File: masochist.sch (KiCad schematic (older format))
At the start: 76 parts, among them J1 USB_C_Receptacle_USB2.0, J2 AVR-ISP-6, SW1 RESET, SW2 SW_Push, U1 ATmega328P-PU, Y1 Crystal

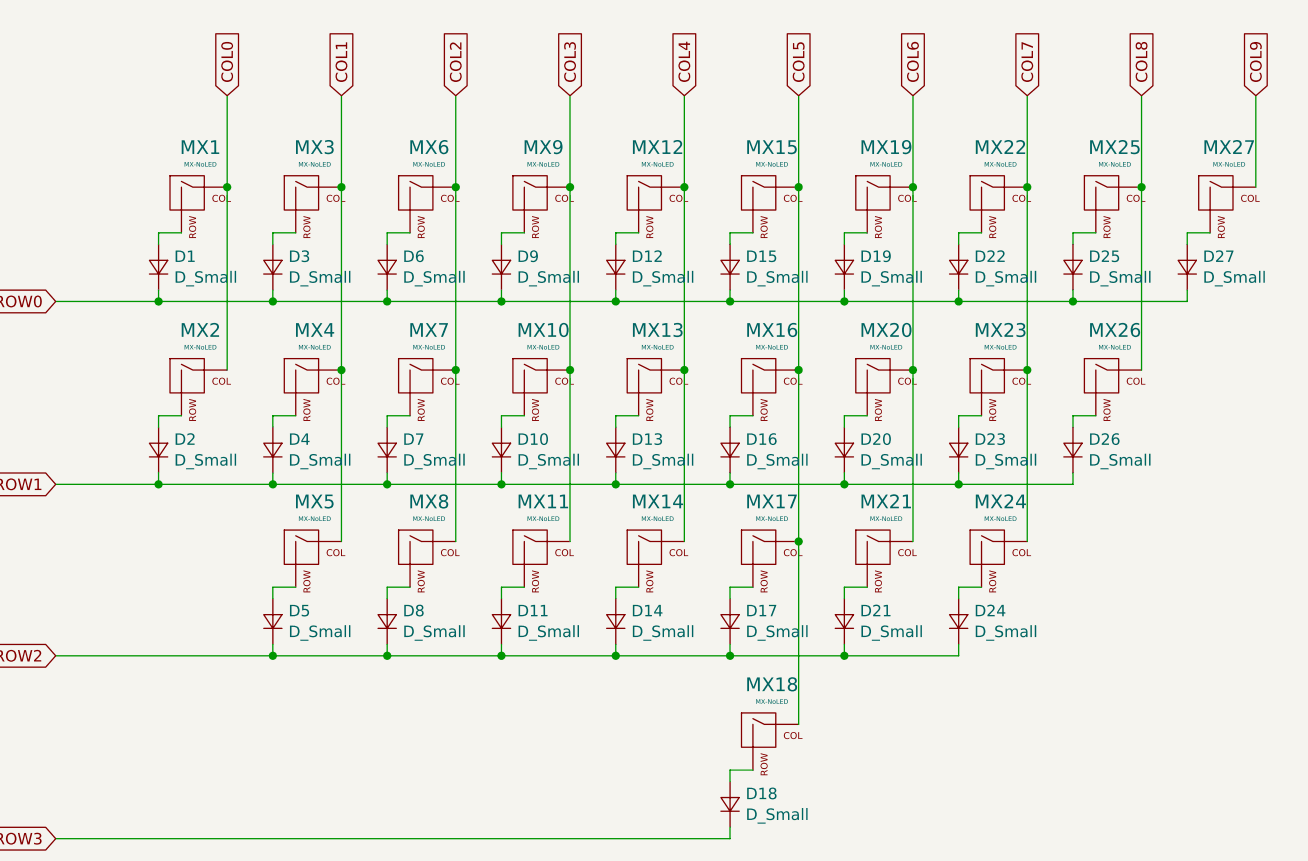
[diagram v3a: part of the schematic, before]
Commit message: laying out the switches and diodes
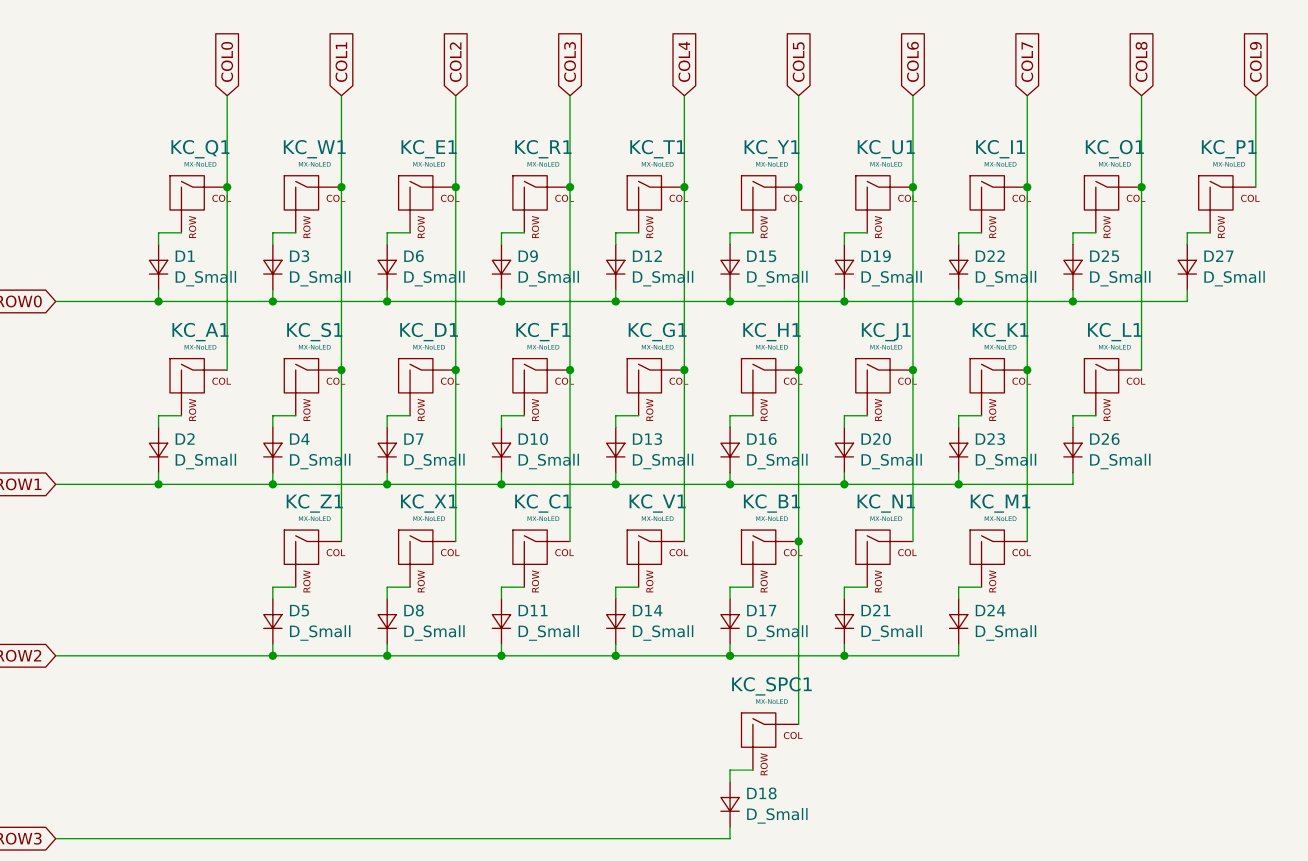
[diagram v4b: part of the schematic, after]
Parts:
- renumbered MX2 to KC_A1, MX17 to KC_B1, MX11 to KC_C1, MX7 to KC_D1, MX6 to KC_E1, MX10 to KC_F1, MX13 to KC_G1, MX16 to KC_H1, MX22 to KC_I1, MX20 to KC_J1, MX23 to KC_K1, MX26 to KC_L1, MX24 to KC_M1, MX21 to KC_N1, MX25 to KC_O1, MX27 to KC_P1, MX1 to KC_Q1, MX9 to KC_R1, MX4 to KC_S1, MX18 to KC_SPC1, MX12 to KC_T1, MX19 to KC_U1, MX14 to KC_V1, MX3 to KC_W1, MX8 to KC_X1, MX15 to KC_Y1, MX5 to KC_Z1
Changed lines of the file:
@@
 	1500 3900 1500 4050
 $Comp
-L MX_Alps_Hybrid:MX-NoLED MX1
+L MX_Alps_Hybrid:MX-NoLED KC_Q1
 U 1 1 5EC3FB15
 P 6450 1200
-F 0 "MX1" H 6483 1423 60  0000 C CNN
+F 0 "KC_Q1" H 6483 1423 60  0000 C CNN
 F 1 "MX-NoLED" H 6483 1349 20  0000 C CNN
 F 2 "cftkb:SW_Cherry_MX1A_1.00u_PCB-NOSCREEN" H 5825 1175 60  0001 C CNN
@@
 	6300 1350 6400 1350
 $Comp
-L MX_Alps_Hybrid:MX-NoLED MX3
+L MX_Alps_Hybrid:MX-NoLED KC_W1
 U 1 1 5EC70529
 P 6950 1200
-F 0 "MX3" H 6983 1423 60  0000 C CNN
+F 0 "KC_W1" H 6983 1423 60  0000 C CNN
 F 1 "MX-NoLED" H 6983 1349 20  0000 C CNN
 F 2 "cftkb:SW_Cherry_MX1A_1.00u_PCB-NOSCREEN" H 6325 1175 60  0001 C CNN
@@
 	6800 1350 6900 1350
 $Comp
-L MX_Alps_Hybrid:MX-NoLED MX6
+L MX_Alps_Hybrid:MX-NoLED KC_E1
 U 1 1 5EC71EA7
 P 7450 1200
-F 0 "MX6" H 7483 1423 60  0000 C CNN
+F 0 "KC_E1" H 7483 1423 60  0000 C CNN
 F 1 "MX-NoLED" H 7483 1349 20  0000 C CNN
 F 2 "cftkb:SW_Cherry_MX1A_1.00u_PCB-NOSCREEN" H 6825 1175 60  0001 C CNN
@@
 	7300 1350 7400 1350
 $Comp
-L MX_Alps_Hybrid:MX-NoLED MX9
+L MX_Alps_Hybrid:MX-NoLED KC_R1
 U 1 1 5EC71EB5
 P 7950 1200
-F 0 "MX9" H 7983 1423 60  0000 C CNN
+F 0 "KC_R1" H 7983 1423 60  0000 C CNN
 F 1 "MX-NoLED" H 7983 1349 20  0000 C CNN
 F 2 "cftkb:SW_Cherry_MX1A_1.00u_PCB-NOSCREEN" H 7325 1175 60  0001 C CNN
@@
 	7800 1350 7900 1350
 $Comp
-L MX_Alps_Hybrid:MX-NoLED MX12
+L MX_Alps_Hybrid:MX-NoLED KC_T1
 U 1 1 5EC74ECF
 P 8450 1200
-F 0 "MX12" H 8483 1423 60  0000 C CNN
+F 0 "KC_T1" H 8483 1423 60  0000 C CNN
 F 1 "MX-NoLED" H 8483 1349 20  0000 C CNN
 F 2 "cftkb:SW_Cherry_MX1A_1.00u_PCB-NOSCREEN" H 7825 1175 60  0001 C CNN
@@
 	8300 1350 8400 1350
 $Comp
-L MX_Alps_Hybrid:MX-NoLED MX15
+L MX_Alps_Hybrid:MX-NoLED KC_Y1
 U 1 1 5EC74EDD
 P 8950 1200
-F 0 "MX15" H 8983 1423 60  0000 C CNN
+F 0 "KC_Y1" H 8983 1423 60  0000 C CNN
 F 1 "MX-NoLED" H 8983 1349 20  0000 C CNN
 F 2 "cftkb:SW_Cherry_MX1A_1.00u_PCB-NOSCREEN" H 8325 1175 60  0001 C CNN
@@
 	8800 1350 8900 1350
 $Comp
-L MX_Alps_Hybrid:MX-NoLED MX19
+L MX_Alps_Hybrid:MX-NoLED KC_U1
 U 1 1 5EC74EEB
 P 9450 1200
-F 0 "MX19" H 9483 1423 60  0000 C CNN
+F 0 "KC_U1" H 9483 1423 60  0000 C CNN
 F 1 "MX-NoLED" H 9483 1349 20  0000 C CNN
 F 2 "cftkb:SW_Cherry_MX1A_1.00u_PCB-NOSCREEN" H 8825 1175 60  0001 C CNN
@@
 	9300 1350 9400 1350
 $Comp
-L MX_Alps_Hybrid:MX-NoLED MX22
+L MX_Alps_Hybrid:MX-NoLED KC_I1
 U 1 1 5EC74EF9
 P 9950 1200
-F 0 "MX22" H 9983 1423 60  0000 C CNN
+F 0 "KC_I1" H 9983 1423 60  0000 C CNN
 F 1 "MX-NoLED" H 9983 1349 20  0000 C CNN
 F 2 "cftkb:SW_Cherry_MX1A_1.00u_PCB-NOSCREEN" H 9325 1175 60  0001 C CNN
@@
 	9800 1350 9900 1350
 $Comp
-L MX_Alps_Hybrid:MX-NoLED MX25
+L MX_Alps_Hybrid:MX-NoLED KC_O1
 U 1 1 5EC76445
 P 10450 1200
-F 0 "MX25" H 10483 1423 60  0000 C CNN
+F 0 "KC_O1" H 10483 1423 60  0000 C CNN
 F 1 "MX-NoLED" H 10483 1349 20  0000 C CNN
 F 2 "cftkb:SW_Cherry_MX1A_1.00u_PCB-NOSCREEN" H 9825 1175 60  0001 C CNN
@@
 	10300 1350 10400 1350
 $Comp
-L MX_Alps_Hybrid:MX-NoLED MX27
+L MX_Alps_Hybrid:MX-NoLED KC_P1
 U 1 1 5EC76453
 P 10950 1200
-F 0 "MX27" H 10983 1423 60  0000 C CNN
+F 0 "KC_P1" H 10983 1423 60  0000 C CNN
 F 1 "MX-NoLED" H 10983 1349 20  0000 C CNN
 F 2 "cftkb:SW_Cherry_MX1A_1.00u_PCB-NOSCREEN" H 10325 1175 60  0001 C CNN
@@
 	10800 1350 10900 1350
 $Comp
-L MX_Alps_Hybrid:MX-NoLED MX2
+L MX_Alps_Hybrid:MX-NoLED KC_A1
 U 1 1 5EC84E7F
 P 6450 2000
-F 0 "MX2" H 6483 2223 60  0000 C CNN
+F 0 "KC_A1" H 6483 2223 60  0000 C CNN
 F 1 "MX-NoLED" H 6483 2149 20  0000 C CNN
 F 2 "cftkb:SW_Cherry_MX1A_1.00u_PCB-NOSCREEN" H 5825 1975 60  0001 C CNN
@@
 	6300 2150 6400 2150
 $Comp
-L MX_Alps_Hybrid:MX-NoLED MX4
+L MX_Alps_Hybrid:MX-NoLED KC_S1
 U 1 1 5EC84E8D
 P 6950 2000
-F 0 "MX4" H 6983 2223 60  0000 C CNN
+F 0 "KC_S1" H 6983 2223 60  0000 C CNN
 F 1 "MX-NoLED" H 6983 2149 20  0000 C CNN
 F 2 "cftkb:SW_Cherry_MX1A_1.00u_PCB-NOSCREEN" H 6325 1975 60  0001 C CNN
@@
 	6800 2150 6900 2150
 $Comp
-L MX_Alps_Hybrid:MX-NoLED MX7
+L MX_Alps_Hybrid:MX-NoLED KC_D1
 U 1 1 5EC84E9B
 P 7450 2000
-F 0 "MX7" H 7483 2223 60  0000 C CNN
+F 0 "KC_D1" H 7483 2223 60  0000 C CNN
 F 1 "MX-NoLED" H 7483 2149 20  0000 C CNN
 F 2 "cftkb:SW_Cherry_MX1A_1.00u_PCB-NOSCREEN" H 6825 1975 60  0001 C CNN
@@
 	7300 2150 7400 2150
 $Comp
-L MX_Alps_Hybrid:MX-NoLED MX10
+L MX_Alps_Hybrid:MX-NoLED KC_F1
 U 1 1 5EC84EA9
 P 7950 2000
-F 0 "MX10" H 7983 2223 60  0000 C CNN
+F 0 "KC_F1" H 7983 2223 60  0000 C CNN
 F 1 "MX-NoLED" H 7983 2149 20  0000 C CNN
 F 2 "cftkb:SW_Cherry_MX1A_1.00u_PCB-NOSCREEN" H 7325 1975 60  0001 C CNN
@@
 	7800 2150 7900 2150
 $Comp
-L MX_Alps_Hybrid:MX-NoLED MX13
+L MX_Alps_Hybrid:MX-NoLED KC_G1
 U 1 1 5EC84EB7
 P 8450 2000
-F 0 "MX13" H 8483 2223 60  0000 C CNN
+F 0 "KC_G1" H 8483 2223 60  0000 C CNN
 F 1 "MX-NoLED" H 8483 2149 20  0000 C CNN
 F 2 "cftkb:SW_Cherry_MX1A_1.00u_PCB-NOSCREEN" H 7825 1975 60  0001 C CNN
@@
 	8300 2150 8400 2150
 $Comp
-L MX_Alps_Hybrid:MX-NoLED MX16
+L MX_Alps_Hybrid:MX-NoLED KC_H1
 U 1 1 5EC84EC5
 P 8950 2000
-F 0 "MX16" H 8983 2223 60  0000 C CNN
+F 0 "KC_H1" H 8983 2223 60  0000 C CNN
 F 1 "MX-NoLED" H 8983 2149 20  0000 C CNN
 F 2 "cftkb:SW_Cherry_MX1A_1.00u_PCB-NOSCREEN" H 8325 1975 60  0001 C CNN
@@
 	8800 2150 8900 2150
 $Comp
-L MX_Alps_Hybrid:MX-NoLED MX20
+L MX_Alps_Hybrid:MX-NoLED KC_J1
 U 1 1 5EC84ED3
 P 9450 2000
-F 0 "MX20" H 9483 2223 60  0000 C CNN
+F 0 "KC_J1" H 9483 2223 60  0000 C CNN
 F 1 "MX-NoLED" H 9483 2149 20  0000 C CNN
 F 2 "cftkb:SW_Cherry_MX1A_1.00u_PCB-NOSCREEN" H 8825 1975 60  0001 C CNN
@@
 	9300 2150 9400 2150
 $Comp
-L MX_Alps_Hybrid:MX-NoLED MX23
+L MX_Alps_Hybrid:MX-NoLED KC_K1
 U 1 1 5EC84EE1
 P 9950 2000
-F 0 "MX23" H 9983 2223 60  0000 C CNN
+F 0 "KC_K1" H 9983 2223 60  0000 C CNN
 F 1 "MX-NoLED" H 9983 2149 20  0000 C CNN
 F 2 "cftkb:SW_Cherry_MX1A_1.00u_PCB-NOSCREEN" H 9325 1975 60  0001 C CNN
@@
 	9800 2150 9900 2150
 $Comp
-L MX_Alps_Hybrid:MX-NoLED MX26
+L MX_Alps_Hybrid:MX-NoLED KC_L1
 U 1 1 5EC84EEF
 P 10450 2000
-F 0 "MX26" H 10483 2223 60  0000 C CNN
+F 0 "KC_L1" H 10483 2223 60  0000 C CNN
 F 1 "MX-NoLED" H 10483 2149 20  0000 C CNN
 F 2 "cftkb:SW_Cherry_MX1A_1.00u_PCB-NOSCREEN" H 9825 1975 60  0001 C CNN
@@
 	10300 2200 10300 2150
 $Comp
-L MX_Alps_Hybrid:MX-NoLED MX5
+L MX_Alps_Hybrid:MX-NoLED KC_Z1
 U 1 1 5EC9C168
 P 6950 2750
-F 0 "MX5" H 6983 2973 60  0000 C CNN
+F 0 "KC_Z1" H 6983 2973 60  0000 C CNN
 F 1 "MX-NoLED" H 6983 2899 20  0000 C CNN
 F 2 "cftkb:SW_Cherry_MX1A_1.00u_PCB-NOSCREEN" H 6325 2725 60  0001 C CNN
@@
 	6800 2900 6900 2900
 $Comp
-L MX_Alps_Hybrid:MX-NoLED MX8
+L MX_Alps_Hybrid:MX-NoLED KC_X1
 U 1 1 5EC9C176
 P 7450 2750
-F 0 "MX8" H 7483 2973 60  0000 C CNN
+F 0 "KC_X1" H 7483 2973 60  0000 C CNN
 F 1 "MX-NoLED" H 7483 2899 20  0000 C CNN
 F 2 "cftkb:SW_Cherry_MX1A_1.00u_PCB-NOSCREEN" H 6825 2725 60  0001 C CNN
@@
 	7300 2900 7400 2900
 $Comp
-L MX_Alps_Hybrid:MX-NoLED MX11
+L MX_Alps_Hybrid:MX-NoLED KC_C1
 U 1 1 5EC9C184
 P 7950 2750
-F 0 "MX11" H 7983 2973 60  0000 C CNN
+F 0 "KC_C1" H 7983 2973 60  0000 C CNN
 F 1 "MX-NoLED" H 7983 2899 20  0000 C CNN
 F 2 "cftkb:SW_Cherry_MX1A_1.00u_PCB-NOSCREEN" H 7325 2725 60  0001 C CNN
@@
 	7800 2900 7900 2900
 $Comp
-L MX_Alps_Hybrid:MX-NoLED MX14
+L MX_Alps_Hybrid:MX-NoLED KC_V1
 U 1 1 5EC9C192
 P 8450 2750
-F 0 "MX14" H 8483 2973 60  0000 C CNN
+F 0 "KC_V1" H 8483 2973 60  0000 C CNN
 F 1 "MX-NoLED" H 8483 2899 20  0000 C CNN
 F 2 "cftkb:SW_Cherry_MX1A_1.00u_PCB-NOSCREEN" H 7825 2725 60  0001 C CNN
@@
 	8300 2900 8400 2900
 $Comp
-L MX_Alps_Hybrid:MX-NoLED MX17
+L MX_Alps_Hybrid:MX-NoLED KC_B1
 U 1 1 5EC9C1A0
 P 8950 2750
-F 0 "MX17" H 8983 2973 60  0000 C CNN
+F 0 "KC_B1" H 8983 2973 60  0000 C CNN
 F 1 "MX-NoLED" H 8983 2899 20  0000 C CNN
 F 2 "cftkb:SW_Cherry_MX1A_1.00u_PCB-NOSCREEN" H 8325 2725 60  0001 C CNN
@@
 	8800 2900 8900 2900
 $Comp
-L MX_Alps_Hybrid:MX-NoLED MX21
+L MX_Alps_Hybrid:MX-NoLED KC_N1
 U 1 1 5EC9C1AE
 P 9450 2750
-F 0 "MX21" H 9483 2973 60  0000 C CNN
+F 0 "KC_N1" H 9483 2973 60  0000 C CNN
 F 1 "MX-NoLED" H 9483 2899 20  0000 C CNN
 F 2 "cftkb:SW_Cherry_MX1A_1.00u_PCB-NOSCREEN" H 8825 2725 60  0001 C CNN
@@
 	9300 2900 9400 2900
 $Comp
-L MX_Alps_Hybrid:MX-NoLED MX24
+L MX_Alps_Hybrid:MX-NoLED KC_M1
 U 1 1 5EC9C1BC
 P 9950 2750
-F 0 "MX24" H 9983 2973 60  0000 C CNN
+F 0 "KC_M1" H 9983 2973 60  0000 C CNN
 F 1 "MX-NoLED" H 9983 2899 20  0000 C CNN
 F 2 "cftkb:SW_Cherry_MX1A_1.00u_PCB-NOSCREEN" H 9325 2725 60  0001 C CNN
@@
 	9800 3200 9300 3200
 $Comp
-L MX_Alps_Hybrid:MX-NoLED MX18
+L MX_Alps_Hybrid:MX-NoLED KC_SPC1
 U 1 1 5ECAC523
 P 8950 3550
-F 0 "MX18" H 8983 3773 60  0000 C CNN
+F 0 "KC_SPC1" H 8983 3773 60  0000 C CNN
 F 1 "MX-NoLED" H 8983 3699 20  0000 C CNN
 F 2 "cftkb:SW_Cherry_MX1A_1.00u_PCB-NOSCREEN" H 8325 3525 60  0001 C CNN

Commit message: Project is NOT dead, components are roughly in place
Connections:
- net D+: now also U1.4 (PD2)
- net D-: now also U1.5 (PD3)
- no-connect marks 8 -> 6
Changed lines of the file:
@@
 $EndDescr
-$Comp
-L MCU_Microchip_ATmega:ATmega328P-PU U1
-U 1 1 5EC3BFE1
-P 1500 2400
-F 0 "U1" H 856 2446 50  0000 R CNN
-F 1 "ATmega328P-PU" H 856 2355 50  0000 R CNN
-F 2 "Package_DIP:DIP-28_W7.62mm" H 1500 2400 50  0001 C CIN
-F 3 "http://ww1.microchip.com/downloads/en/DeviceDoc/ATmega328_P%20AVR%20MCU%20with%20picoPower%20Technology%20Data%20Sheet%2040001984A.pdf" H 1500 2400 50  0001 C CNN
-	1    1500 2400
-	1    0    0    -1
-$EndComp
 $Comp
 L power:GND #PWR0101
@@
 NoConn ~ 2100 3500
 NoConn ~ 2100 3400
-NoConn ~ 2100 3200
-NoConn ~ 2100 3100
 NoConn ~ 900  1200
+$Comp
+L MCU_Microchip_ATmega:ATmega328P-PU U1
+U 1 1 5EC3BFE1
+P 1500 2400
+F 0 "U1" H 856 2446 50  0000 R CNN
+F 1 "ATmega328P-PU" H 856 2355 50  0000 R CNN
+F 2 "Package_DIP:DIP-28_W7.62mm" H 1500 2400 50  0001 C CIN
+F 3 "http://ww1.microchip.com/downloads/en/DeviceDoc/ATmega328_P%20AVR%20MCU%20with%20picoPower%20Technology%20Data%20Sheet%2040001984A.pdf" H 1500 2400 50  0001 C CNN
+	1    1500 2400
+	1    0    0    -1
+$EndComp
+Text GLabel 2100 3100 2    50   Input ~ 0
+D+
+Text GLabel 2100 3200 2    50   Input ~ 0
+D-
 $EndSCHEMATC

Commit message: More traces (switches and matrix diodes)
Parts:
- KC_SPC1: footprint cftkb:SW_Cherry_MX1A_1.00u_PCB-NOSCREEN -> MX_Only:MXOnly-6.25U-NoLED
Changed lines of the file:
@@
 F 0 "KC_SPC1" H 8983 3773 60  0000 C CNN
 F 1 "MX-NoLED" H 8983 3699 20  0000 C CNN
-F 2 "cftkb:SW_Cherry_MX1A_1.00u_PCB-NOSCREEN" H 8325 3525 60  0001 C CNN
+F 2 "MX_Only:MXOnly-6.25U-NoLED" H 8325 3525 60  0001 C CNN
 F 3 "" H 8325 3525 60  0001 C CNN
 	1    8950 3550

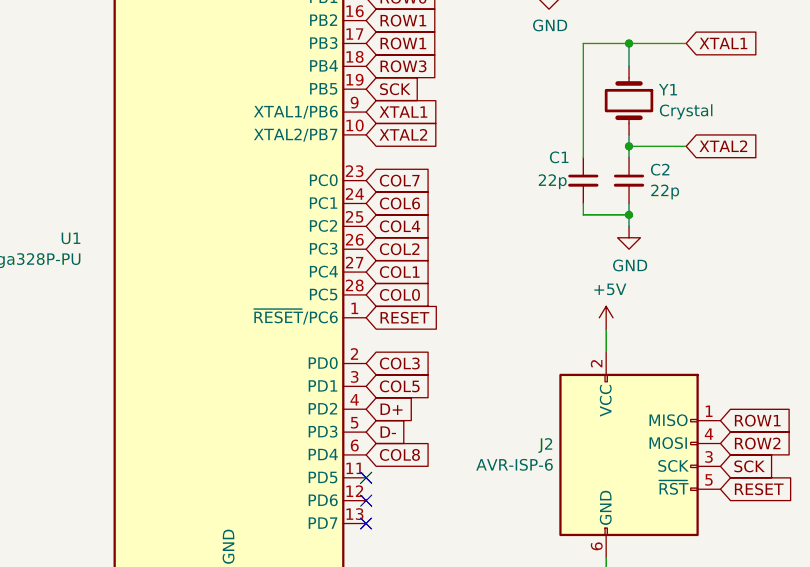
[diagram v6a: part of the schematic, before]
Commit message: reassigning pins to hopefully make routing easier
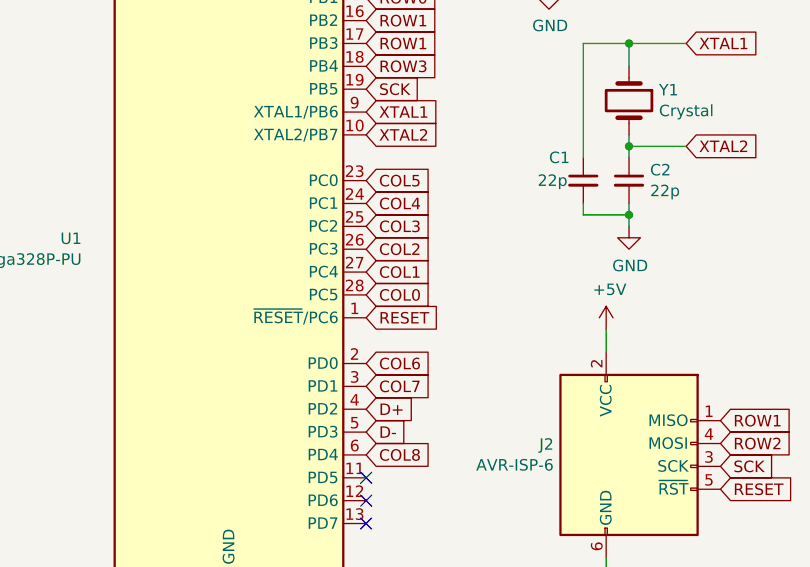
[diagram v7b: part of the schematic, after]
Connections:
- net COL3: now also U1.25 (PC2); no longer U1.2 (PD0)
- net COL4: now also U1.24 (PC1); no longer U1.25 (PC2)
- net COL5: now also U1.23 (PC0); no longer U1.3 (PD1)
- net COL6: now also U1.2 (PD0); no longer U1.24 (PC1)
- net COL7: now also U1.3 (PD1); no longer U1.23 (PC0)
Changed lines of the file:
@@
 Text GLabel 2100 2400 2    50   Input ~ 0
 COL2
-Text GLabel 2100 2300 2    50   Input ~ 0
-COL4
-Text GLabel 2100 2200 2    50   Input ~ 0
+Text GLabel 2100 2900 2    50   Input ~ 0
 COL6
-Text GLabel 2100 2100 2    50   Input ~ 0
+Text GLabel 2100 3000 2    50   Input ~ 0
 COL7
-Text GLabel 2100 2900 2    50   Input ~ 0
-COL3
-Text GLabel 2100 3000 2    50   Input ~ 0
-COL5
 Text GLabel 2100 3300 2    50   Input ~ 0
 COL8
@@
 Text GLabel 2100 3200 2    50   Input ~ 0
 D-
+Text GLabel 2100 2100 2    50   Input ~ 0
+COL5
+Text GLabel 2100 2200 2    50   Input ~ 0
+COL4
+Text GLabel 2100 2300 2    50   Input ~ 0
+COL3
 $EndSCHEMATC

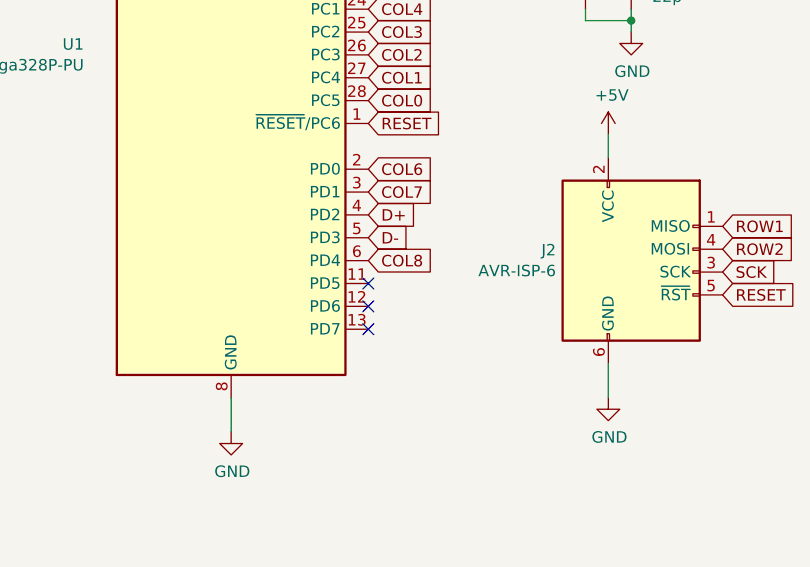
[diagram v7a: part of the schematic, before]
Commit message: Forgot to connect the BOOT switch to anything in the schematic
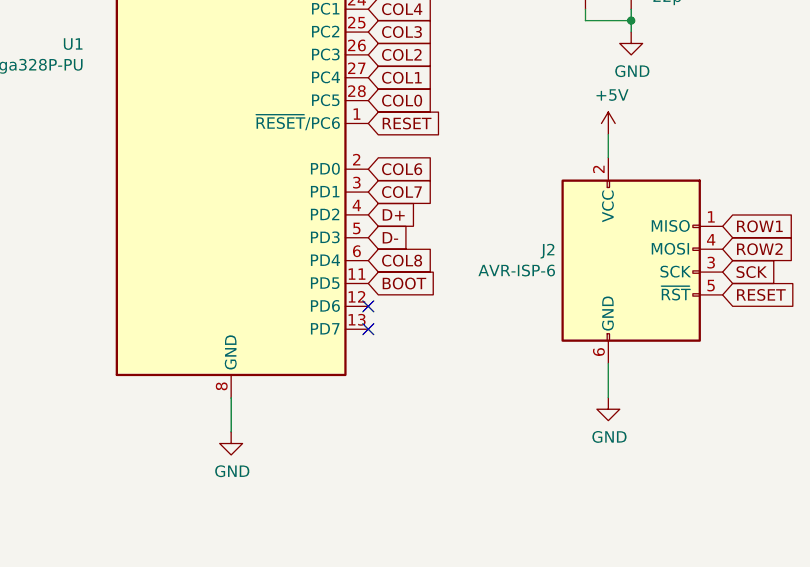
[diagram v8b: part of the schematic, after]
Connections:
- net BOOT: now also U1.11 (PD5)
- no-connect marks 6 -> 5
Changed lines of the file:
@@
 NoConn ~ 2100 3600
 NoConn ~ 2100 3500
-NoConn ~ 2100 3400
 NoConn ~ 900  1200
+Text GLabel 2100 3100 2    50   Input ~ 0
+D+
+Text GLabel 2100 3200 2    50   Input ~ 0
+D-
+Text GLabel 2100 2100 2    50   Input ~ 0
+COL5
+Text GLabel 2100 2200 2    50   Input ~ 0
+COL4
+Text GLabel 2100 2300 2    50   Input ~ 0
+COL3
 $Comp
 L MCU_Microchip_ATmega:ATmega328P-PU U1
@@
 	1    0    0    -1
 $EndComp
-Text GLabel 2100 3100 2    50   Input ~ 0
-D+
-Text GLabel 2100 3200 2    50   Input ~ 0
-D-
-Text GLabel 2100 2100 2    50   Input ~ 0
-COL5
-Text GLabel 2100 2200 2    50   Input ~ 0
-COL4
-Text GLabel 2100 2300 2    50   Input ~ 0
-COL3
+Text GLabel 2100 3400 2    50   Input ~ 0
+BOOT
 $EndSCHEMATC
